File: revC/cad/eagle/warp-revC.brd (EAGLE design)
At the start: 38.1 x 38.1 mm, 143 parts, among them J2 QIIC connector, J3 QIIC connector, J4 DF40FC-20DP-0.4V(51), J5 CORTEX_DEBUG_SMD, U1 MAX40200, U2 MAX40200

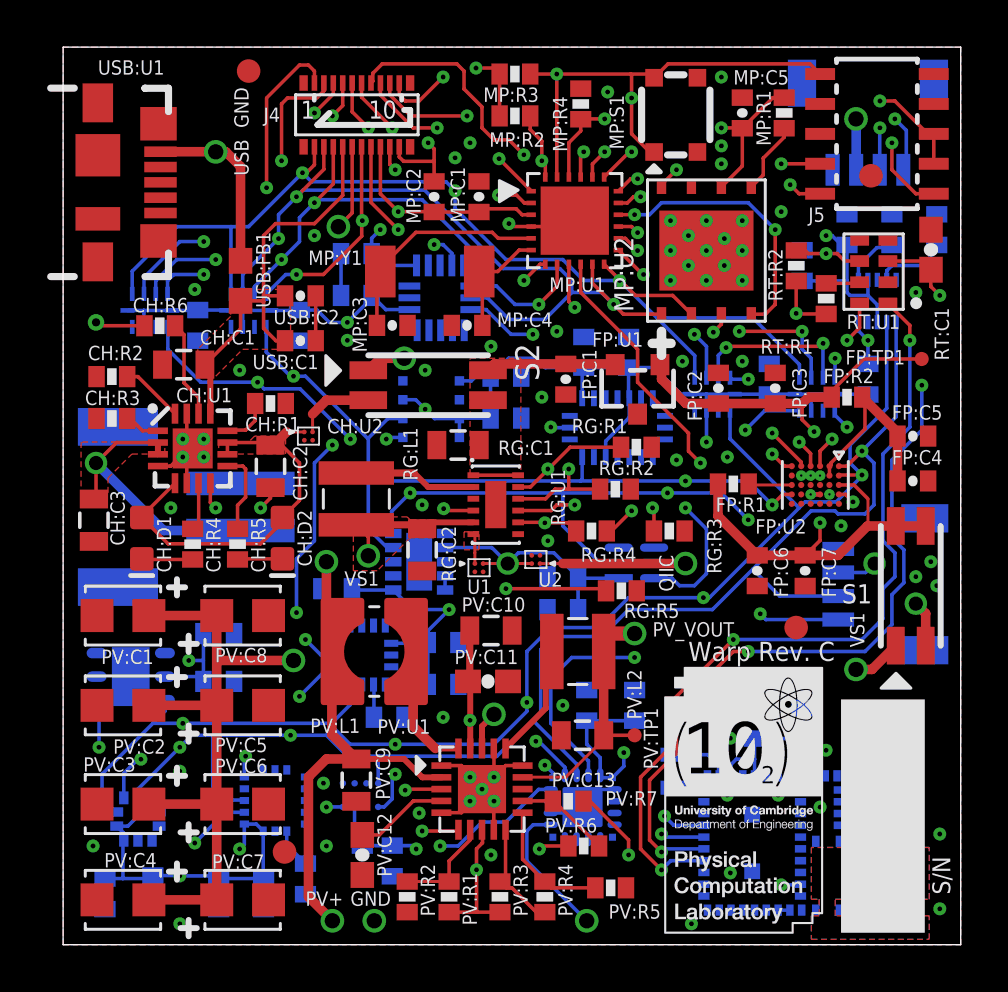
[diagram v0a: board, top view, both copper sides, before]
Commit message: Rerouted FPGA
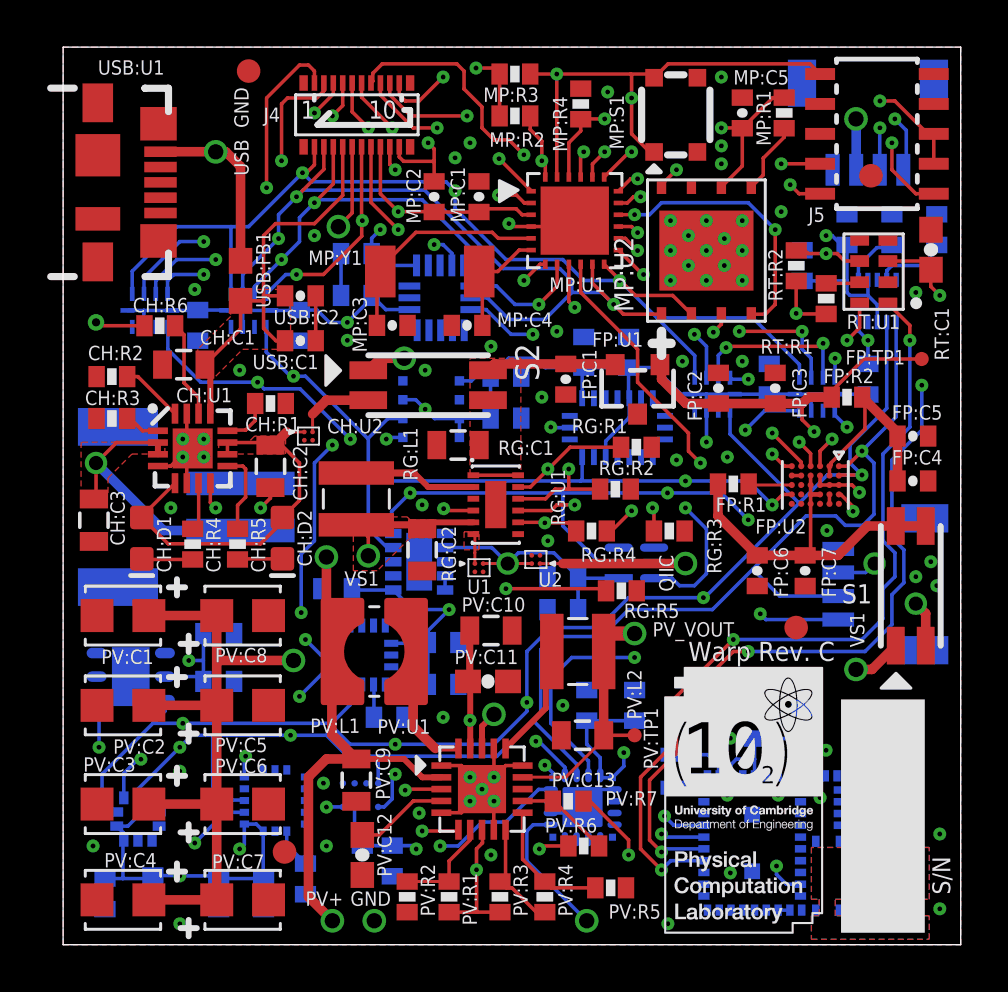
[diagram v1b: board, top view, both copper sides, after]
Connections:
- net FP:VCC_1V2: now also FP:U2.A3, FP:U2.B3, FP:U2.C3
- net FPGA_VS: now also FP:U2.D3, FP:U2.D5; no longer FP:U2.A3
- net GND: now also FP:U2.B5, FP:U2.F2
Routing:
- net FP:VCC_1V2: track 16.5 -> 20.1 mm
- net FPGA_VS: track 18.2 -> 15.3 mm, vias 3 -> 0
- net GND: track 51.4 -> 50.6 mm, vias 80 -> 78
